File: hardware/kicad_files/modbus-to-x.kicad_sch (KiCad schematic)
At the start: 39 parts, among them IC1 ESP32-WROOM-32D_M113DH2800PH3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, J1 615006138421, J4 M50-3140545R, Q1 DSS4160U-7, Q2 DSS4160U-7, SW1 SW_Wuerth_450301014042, SW4 3983, U1 LM2596S-3.3, U3 MAX3485

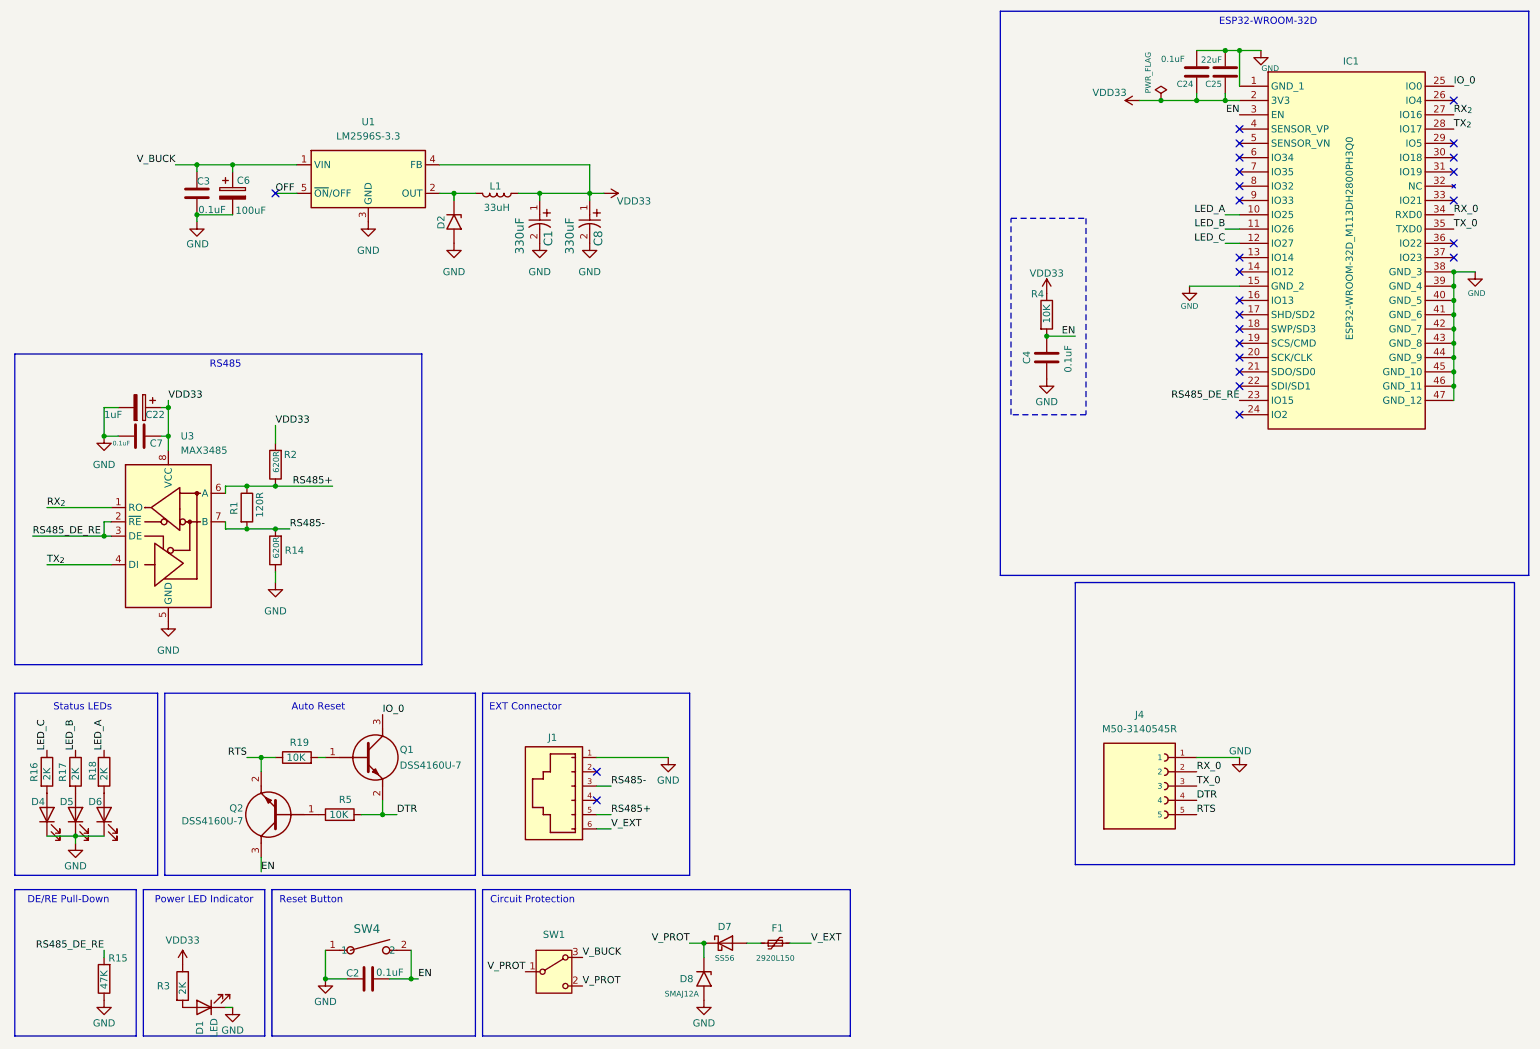
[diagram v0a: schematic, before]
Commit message: - Added Micro USB port - Added header for OpenLog - Minor silkscreen updates - New buck conv. inductor improving cost
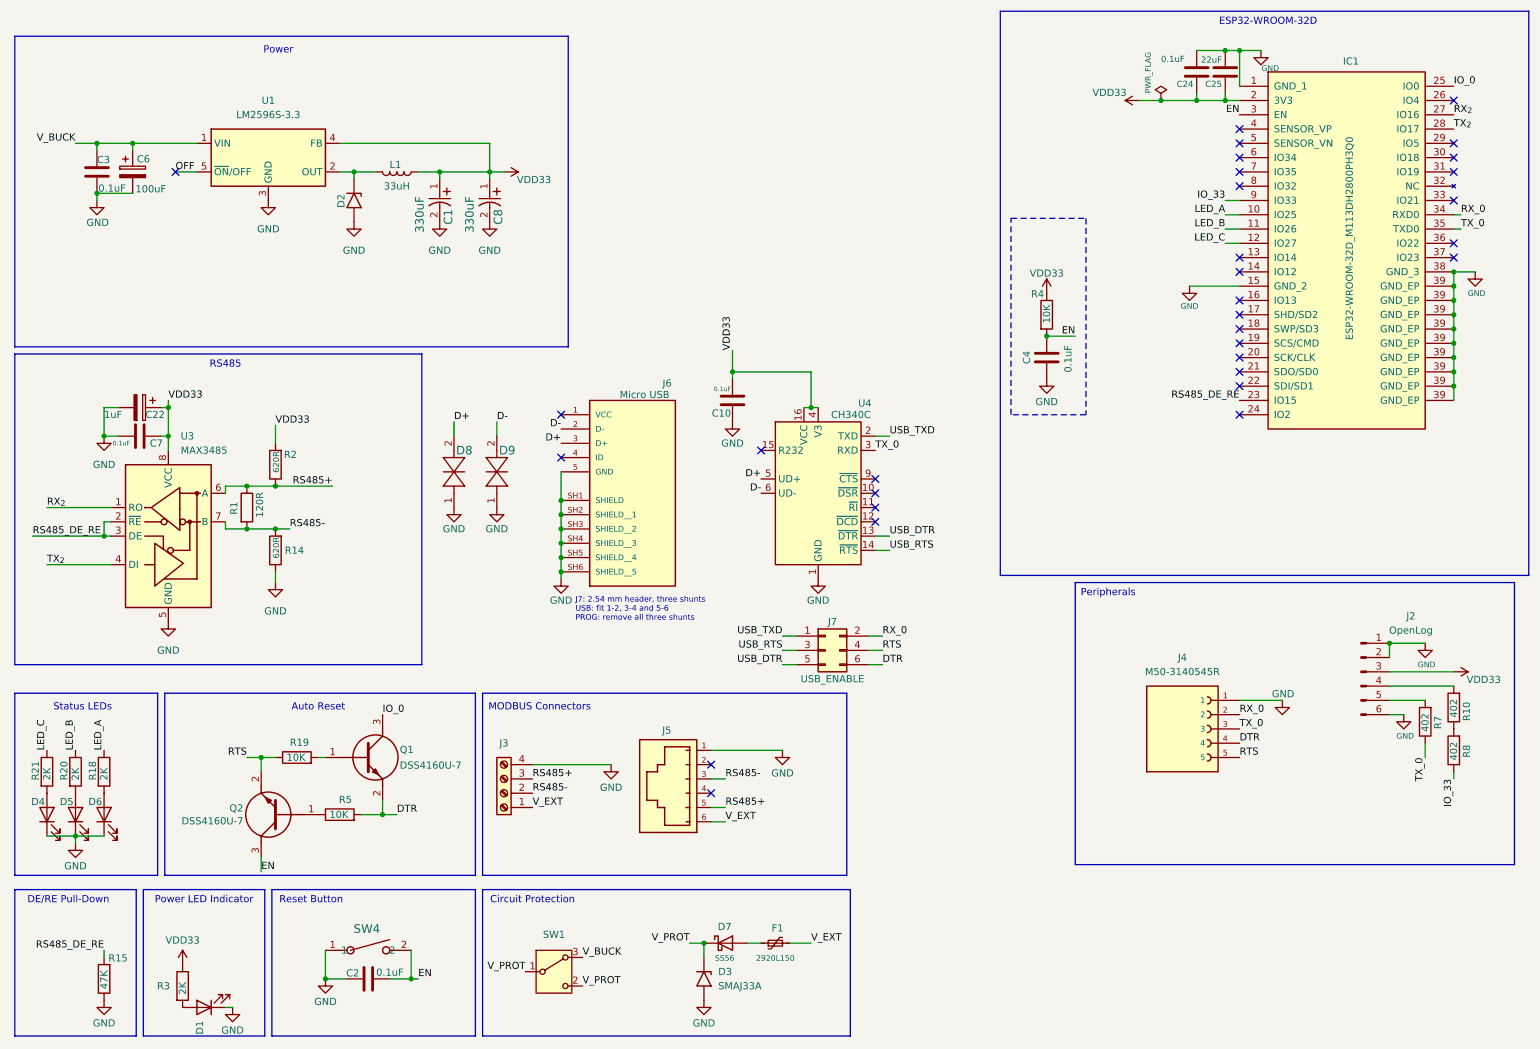
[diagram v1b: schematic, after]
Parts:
- removed D8: SMAJ12A, Diode_SMD:D_SMA, symbol Diode:SMAJ12A
- removed J1: 615006138421, project_footprints:RJ12_615006138421, symbol RJ12_615006138421:615006138421
- removed R16, R17: 2K, Resistor_SMD:R_0603_1608Metric_Pad0.98x0.95mm_HandSolder, symbol Device:R
- added C10: 0.1uF, Capacitor_SMD:C_0805_2012Metric, symbol Device:C
- added D3: SMAJ33A, Diode_SMD:D_SMA, symbol Diode:SMAJ33A
- added D8, D9: PESD0402-140, project_footprints:PESD0402-140_LTF, symbol mbx:PESD0402-140
- added J2: OpenLog, project_footprints:MBX_PinHeader_1x06_P2.54mm_Vertical, symbol Connector:Conn_01x06_Pin
- added J3: Screw_Terminal_01x04, TerminalBlock_Phoenix:TerminalBlock_Phoenix_MKDS-1,5-4-5.08_1x04_P5.08mm_Horizontal, symbol Connector:Screw_Terminal_01x04
- added J5: 615006138421, project_footprints:RJ12_615006138421, symbol project_symbols:615006138421
- added J6: Micro USB, project_footprints:AMPHENOL_10118194-0001LF, symbol project_symbols:10118194-0001LF
- added J7: USB_ENABLE, Connector_PinHeader_2.54mm:PinHeader_2x03_P2.54mm_Vertical, symbol Connector_Generic:Conn_02x03_Odd_Even
- added R10, R7, R8: 402, project_footprints:MBX_R_0402_1005Metric, symbol Device:R
- added R20, R21: 2K, Resistor_SMD:R_0603_1608Metric_Pad0.98x0.95mm_HandSolder, symbol Device:R
- added U4: CH340C, Package_SO:SOIC-16_3.9x9.9mm_P1.27mm, symbol Interface_USB:CH340C
- C1, C8: symbol Tantalum 330uF T495D337K006ATE100:T495D337K006ATE100 -> project_symbols:T495D337K006ATE100; InternalId C #20 -> (none); MPN (none) -> T495D337K006ATE100; Manufacturer (none) -> KEMET; PartNo T495D337K006ATE100 -> (none); StockLocation (none) -> C #20
- C2, C4, C7: InternalId C #39 -> (none); MPN (none) -> GCD21BR71H104KA01L; Manufacturer (none) -> Murata; PartNo GCD21BR71H104KA01L -> (none); StockLocation (none) -> C #39
- C22: InternalId C #35 -> (none); MPN (none) -> NACE1R0M50V4X5.5TR15F; Manufacturer (none) -> NIC Components; PartNo NACE1R0M50V4X5.5TR15F -> (none); StockLocation (none) -> C #35
- C24: InternalId C #39 -> (none); MPN (none) -> GCD21BR71H104KA01L; PartNo GCD21BR71H104KA01L -> (none); StockLocation (none) -> C #39
- C25: InternalId C #17 -> (none); MPN (none) -> CL21A226MOCLRNC; Manufacturer (none) -> Samsung Electro-Mechanics; PartNo CL21A226MOCLRNC -> (none); StockLocation (none) -> C #17
- C3: Id C #TBD -> (none); MPN (none) -> C0603C104K5RACTU; Manufacturer (none) -> KEMET; PartNo C0603C104K5RACTU -> (none); StockLocation (none) -> C #45
- C6: footprint project_footprints:25SVPF100M -> project_footprints:ESY107M050AG3AA; InternalId C #44 -> (none); MPN (none) -> ESY107M050AG3AA; Manufacturer (none) -> KEMET; PartNo 25SVPF100M -> (none); StockLocation (none) -> C #46; Voltage 25V -> 50V
- D1: InternalId Reel -> (none); MPN (none) -> LW QH8G-Q2OO-3K5L-1; Manufacturer (none) -> OSRAM; PartNo LW QH8G-Q2OO-3K5L-1 -> (none); StockLocation (none) -> REEL
- D2: InternalId Dio. #10 -> (none); MPN (none) -> B340LA-13-F; Manufacturer (none) -> Diodes Incorporated; PartNo B340LA-13-F -> (none); StockLocation (none) -> Diodes #10
- D4, D5, D6: InternalId REEL -> (none); MPN (none) -> LW QH8G-Q2OO-3K5L-1; Manufacturer (none) -> OSRAM; PartNo LW QH8G-Q2OO-3K5L-1 -> (none); StockLocation (none) -> REEL
- D7: Id TDB -> (none); MPN (none) -> SS56; Manufacturer (none) -> Slkor; PartNo SS56 -> (none); StockLocation (none) -> Diodes #22
- F1: Id Fuses #TBD -> (none); MPN (none) -> 2920L150/60MR; Manufacturer (none) -> Littelfuse; PartNo 2920L150/60MR -> (none); StockLocation (none) -> Other #13
- IC1: symbol Library:ESP32-WROOM-32D_M113DH2800PH3Q0_ -> project_symbols:ESP32-WROOM-32D_EP39; InternalId IC #48 -> (none); MPN (none) -> M113DH2800PH3Q0; Manufacturer (none) -> Espressif; PartNo M113DH2800PH3Q0 -> (none); StockLocation (none) -> IC #48
- J4: symbol M50-3140545R:M50-3140545R -> project_symbols:M50-3140545R; InternalId Conn. #28 -> (none); MPN (none) -> M50-3140545R; Manufacturer (none) -> Harwin; PartNo M50-3140545R -> (none); StockLocation (none) -> Conn. #28
- L1: footprint project_footprints:7447709330 -> project_footprints:IND_BOURNS_SRR1260; InternalId IND. #25 -> (none); MPN (none) -> SRR1260-330M; Manufacturer (none) -> Bourns; PartNo 7447709330 -> (none); StockLocation (none) -> IND. #26
- Q1, Q2: symbol DSS4160U-7:DSS4160U-7 -> project_symbols:DSS4160U-7; InternalId TRANS #7 -> (none); MPN (none) -> DSS4160U-7; Manufacturer (none) -> Diodes Incorporated; PartNo DSS4160U-7 -> (none); StockLocation (none) -> TRANS #7
- R1: InternalId R #32 -> (none); MPN (none) -> RC1206FR-13120RL; Manufacturer (none) -> Yageo; PartNo RC1206FR-13120RL -> (none); StockLocation (none) -> R #32
- R14, R2: InternalId R #13 -> (none); MPN (none) -> 1550805S8F6200T5E; Manufacturer (none) -> RND; PartNo RND 1550805S8F6200T5E -> (none); StockLocation (none) -> R #13
- R15: InternalId R #24 -> (none); MPN (none) -> 1550805S8F4702T5E; Manufacturer (none) -> RND; PartNo RND 1550805S8F4702T5E -> (none); StockLocation (none) -> R #24
- R18, R3: InternalId R #15 -> (none); MPN (none) -> 155TC0325B2001T5H; Manufacturer (none) -> RND; PartNo RND 155TC0325B2001T5H -> (none); StockLocation (none) -> R #15
- R19, R4, R5: InternalId R #35 -> (none); MPN (none) -> RT0603DRE0710KL; Manufacturer (none) -> Yageo; PartNo RT0603DRE0710KL -> (none); StockLocation (none) -> R #35
- SW1: value SW_Wuerth_450301014042 -> SS12D00G3; InternalId Conn. #23 -> (none); MPN (none) -> SS12D00G3; Manufacturer (none) -> Generic; StockLocation (none) -> Conn. #23
- SW4: symbol Adafruit 3983 Mini Soft Touch Switch:3983 -> project_symbols:3983; InternalId Conn. #27 -> (none); MPN (none) -> Adafruit-3983; Manufacturer (none) -> Adafruit; PartNo Adafruit-3983 -> (none); StockLocation (none) -> Conn. #27
- U1: InternalId IC #43 -> (none); InventoryId (none) -> IC #43; MPN (none) -> LM2596S-3.3-EV; Manufacturer (none) -> EVVO; StockLocation (none) -> IC #43
- U3: InternalId IC #36 -> (none); MPN (none) -> MAX3485CSA+T; Manufacturer (none) -> Analog Devices; PartNo MAX3485CSA+T -> (none); StockLocation (none) -> IC #36
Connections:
- net DTR: now also J7.6 (Pin_6)
- net GND: now also C10.1, D3.2 (A2), D8.1, D9.1, J2.1 (Pin_1), J2.2 (Pin_2), J2.6 (Pin_6), J3.4 (Pin_4), J5.1, J6.5 (GND), J6.SH1 (SHIELD), J6.SH2 (SHIELD__1), J6.SH3 (SHIELD__2), J6.SH4 (SHIELD__3), J6.SH5 (SHIELD__4), J6.SH6 (SHIELD__5), U4.1 (GND); no longer IC1.40 (GND_5), IC1.41 (GND_6), IC1.42 (GND_7), IC1.43 (GND_8), IC1.44 (GND_9), IC1.45 (GND_10), IC1.46 (GND_11), IC1.47 (GND_12)
- net LED_B: now also R20.1
- net LED_C: now also R21.1
- net RS485+: now also J3.3 (Pin_3), J5.5
- net RS485-: now also J3.2 (Pin_2), J5.3
- net RTS: now also J7.4 (Pin_4)
- net RX_0: now also J7.2 (Pin_2)
- net TX_0: now also R7.1, U4.3 (RXD)
- net VDD33: now also C10.2, J2.3 (Pin_3), U4.16 (VCC), U4.4 (V3)
- net V_EXT: now also J3.1 (Pin_1), J5.6
- net V_PROT: now also D3.1 (A1)
- net at D4.2 (A): now also R21.2
- net at D5.2 (A): now also R20.2
- net IO_33: now reaches IC1.9 (IO33)
- net IO_33: now also R8.1
- new net: R10.1, R8.2
- new net: J2.5 (Pin_5), R7.2
- new net: J2.4 (Pin_4), R10.2
- new net D+: D8.2, J6.3 (D+), U4.5 (UD+)
- new net D-: D9.2, J6.2 (D-), U4.6 (UD-)
- new net USB_DTR: J7.5 (Pin_5), U4.13 (~{DTR})
- new net USB_RTS: J7.3 (Pin_3), U4.14 (~{RTS})
- new net USB_TXD: J7.1 (Pin_1), U4.2 (TXD)
- no-connect marks 26 -> 32
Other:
- note added: "J7: 2.54 mm header, three shunts USB: fit 1-2, 3-4 and 5-6 PROG: remove all three shunts"
- note added: "MODBUS Connectors"
- note added: "Peripherals"
- note added: "Power"
- note removed: "EXT Connector"
- moved on the sheet: C1, C3, C6, C8, D2, J4, L1, U1
